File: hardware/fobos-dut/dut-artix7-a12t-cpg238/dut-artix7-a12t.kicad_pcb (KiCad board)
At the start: 4 copper layers, 88.9 x 76.2 mm, 204 parts, among them J1 Target, J10 Barrel_Jack_Switch, J2 Pmod 2x6, J3 575-8, J4 Glitch, J5 Conn_01x02, J6 Measure, J7 0878321420, J8 575-8, J9 Measure, Q1 FDS9435A, Q2 MMBT3904, Q3 BSS138, Q4 BSS138, Q5 BSS138, Q6 BSS138, Q7 BSS138, Q8 MMBT3904, SW1 SW_DIP_x03, SW2 SW_DIP_x03, U1 XC7A12T-CPG238, U10 SP3003-04ATG, U11 SP3003-04ATG, U2 SP3003-04ATG, U3 SP3003-04ATG, U4 SP3003-04ATG, U5 INA225, U6 BGA2801, U7 TS3A5018DBQR, U8 LTC3569EFE#PBF, U9 IS25LP256D-JMLE

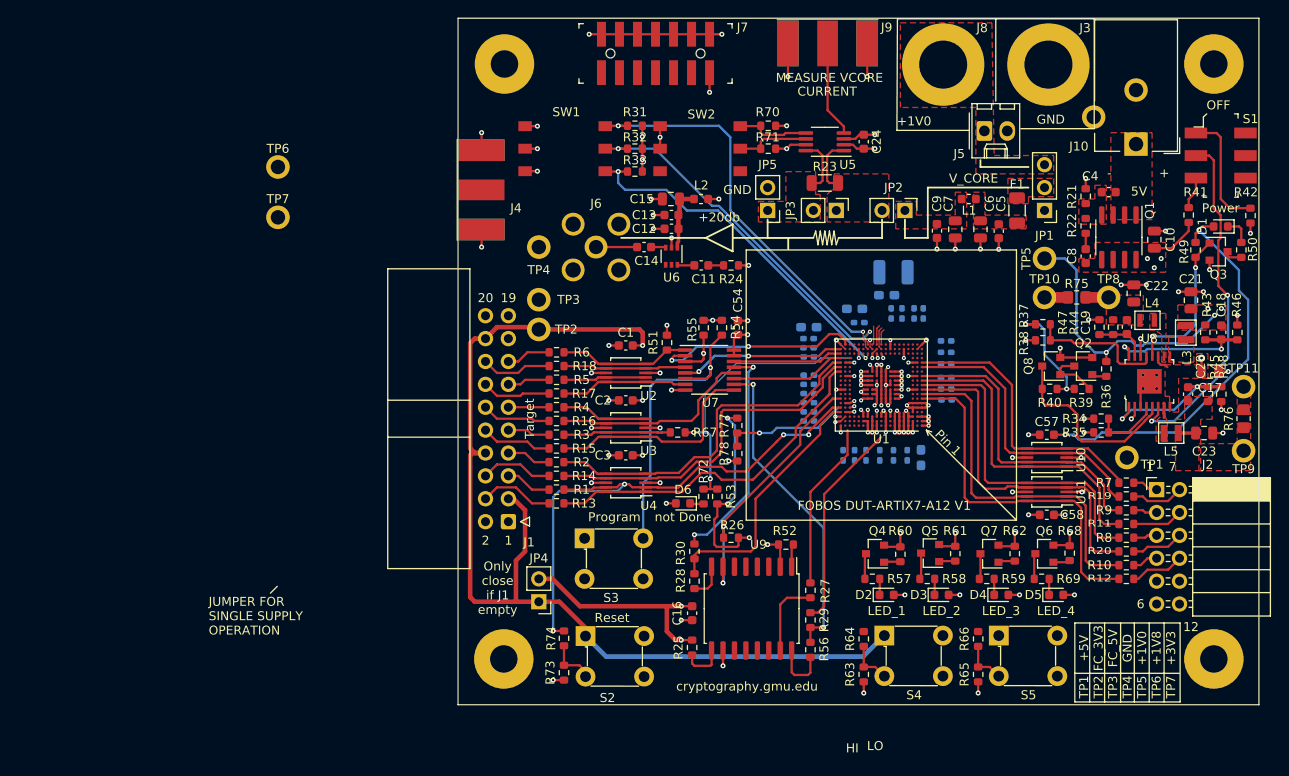
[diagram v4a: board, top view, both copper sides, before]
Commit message: All signals routed, need to route power
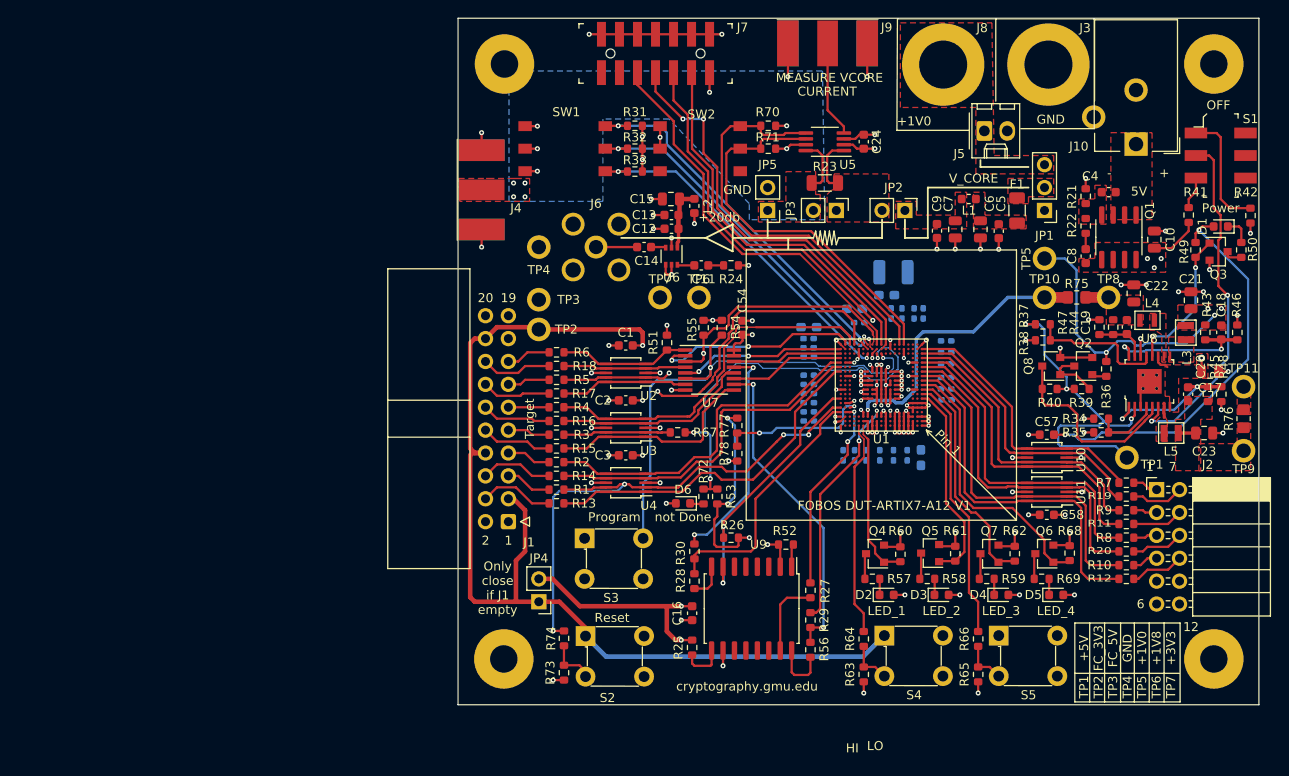
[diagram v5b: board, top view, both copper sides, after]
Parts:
- moved TP6 48.9 mm to (26.7, 27.4)
- moved TP7 43.3 mm to (22.4, 27.4)
- moved L2 1.07 mm to (26.2, 17.2), turned to 90 degrees
- moved C54 0.51 mm to (31.6, 30.7)
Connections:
- J7 pad 8: /FPGA Programming/TDO -> TDO
- R31 pad 2: /FPGA Programming/MODE_0 -> MODE_0
- SW1 pad 2: /FPGA Programming/MODE_0 -> MODE_0
- U1 pad A14: Net-(U1-PadA14) -> USER_LED_1
- U1 pad A15: Net-(U1-PadA15) -> USER_BTN_1
- U1 pad G1: JA10 -> USER_LED_2
- U1 pad H1: JA4 -> USER_BTN_2
- U1 pad J1: JA9 -> USER_LED_3
- U1 pad K1: JA3 -> USER_LED_4
- U1 pad L1: Net-(U1-PadL1) -> JA10
- U1 pad M1: Net-(U1-PadM1) -> JA4
- U1 pad N1: Net-(U1-PadN1) -> JA9
- U1 pad P1: Net-(U1-PadP1) -> JA3
- U1 pad R1: Net-(U1-PadR1) -> JA8
- U1 pad T1: Net-(U1-PadT1) -> JA2
- U1 pad U1: Net-(U1-PadU1) -> JA7
- U1 pad V1: Net-(U1-PadV1) -> JA1
- U1 pad V10: /FPGA Programming/TDO -> TDO
- U1 pad V13: /FPGA Programming/MODE_0 -> MODE_0
- U1 pad W14: Net-(U1-PadW14) -> MODE_0
- U1 pad W16: Net-(U1-PadW16) -> FD2C_HS
- U1 pad W17: Net-(U1-PadW17) -> FC2D_HS
- U1 pad W5: Net-(U1-PadW5) -> VCORE_CURRENT_GAIN_1
- U1 pad W6: Net-(U1-PadW6) -> VCORE_CURRENT_GAIN_0
- U1 pad W9: Net-(U1-PadW9) -> TDO
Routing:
- net +3V3: track 138.0 -> 251.0 mm
- net +1V8: track 6.10 -> 99.5 mm
- net /FPGA Programming/TCK: track 0.66 -> 62.6 mm, vias 1 -> 2
- net TDO: track 0.00 -> 46.5 mm, vias 0 -> 2
- net /FPGA Programming/MODE_0: track 46.0 -> 0.00 mm, vias 2 -> 0
- net /FPGA Programming/TDI: track 2.22 -> 44.9 mm
- net MODE_0: track 0.00 -> 41.4 mm, vias 0 -> 2
- net /FPGA Programming/TMS: track 1.78 -> 42.6 mm
- net VCORE_CURRENT_GAIN_0: track 8.25 -> 45.8 mm
- net FD2C_HS: track 9.17 -> 46.2 mm, vias 0 -> 2
- net VCORE_CURRENT_GAIN_1: track 8.17 -> 43.0 mm
- net FC2D_HS: track 9.60 -> 40.5 mm
- net USER_BTN_2: track 0.00 -> 29.5 mm
- net USER_LED_4: track 1.89 -> 31.0 mm
- net USER_BTN_1: track 0.00 -> 23.9 mm
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- added copper zone on B.Cu, net VCCINT
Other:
- net class Default: clearance 0.0762 -> 0.127
- rule trace_clearance: 0.0762 -> 0.127
- board text removed: "JUMPER FOR SINGLE SUPPLY OPERATION"

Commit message: Traces are routed and DRC errors are cleared, last remaining step is to place L3 power planes
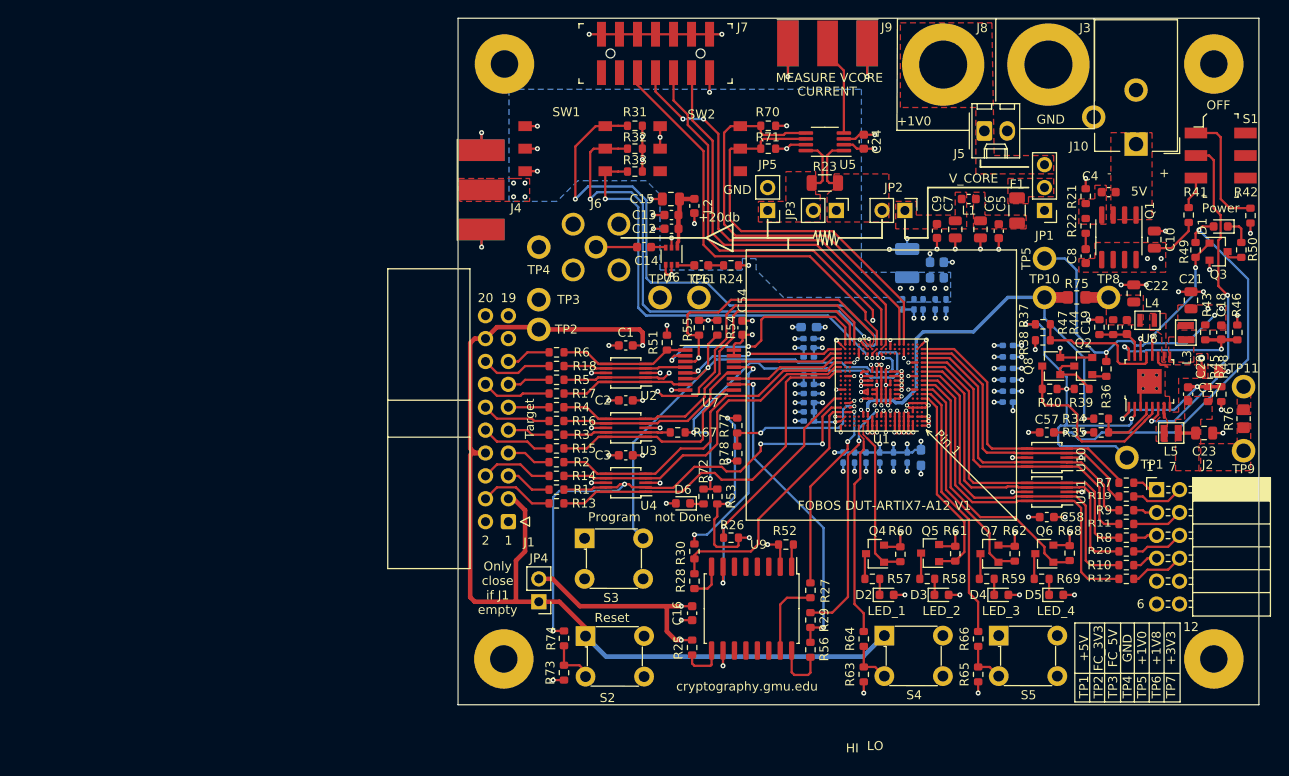
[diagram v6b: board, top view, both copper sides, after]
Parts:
- moved C55 9.42 mm to (52.4, 24.3), turned to 90 degrees
- moved C47 6.93 mm to (53.9, 24.3), turned to 90 degrees
- moved C49 6.88 mm to (61.0, 32.7)
- moved C50 6.88 mm to (61.0, 35.2)
- moved C52 6.88 mm to (61.0, 34.0)
- moved C48 6.86 mm to (61.0, 36.5)
- moved C51 6.86 mm to (61.0, 37.8)
- moved C53 6.80 mm to (61.0, 39.0)
- moved C44 6.16 mm to (54.2, 28.1), turned to 270 degrees
- moved C56 5.23 mm to (49.3, 28.1), turned to 270 degrees
- moved C46 3.83 mm to (53.0, 28.1), turned to 270 degrees
- moved C38 1.82 mm to (49.9, 23.6), turned to 90 degrees
- moved C41 1.44 mm to (50.6, 28.1), turned to 270 degrees
- moved C42 1.41 mm to (51.6, 28.1), turned to 270 degrees
- moved R54 0.51 mm to (28.8, 30.7)
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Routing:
- net +3V3: track 251.0 -> 317.2 mm, vias 23 -> 36
- net GND: track 177.4 -> 219.8 mm, vias 100 -> 129
- net +1V8: track 99.5 -> 126.8 mm, vias 3 -> 6
- net VCCINT: track 20.5 -> 46.8 mm, vias 8 -> 13
- net MODE_0: track 41.4 -> 62.8 mm
- net /FPGA Programming/MODE_1: track 40.7 -> 54.4 mm
- net /FPGA Programming/MODE_2: track 39.0 -> 49.2 mm
- net FC_DIO3_MUX: track 23.0 -> 26.9 mm
- net SW_INIT_B: track 28.1 -> 31.6 mm
- net SW_PROGRAM_B: track 57.3 -> 54.1 mm
- net FC2D_HS: track 40.5 -> 43.5 mm
- net FD2C_CLK: track 39.1 -> 41.6 mm
- net /FPGA Programming/TDI: track 44.9 -> 47.4 mm
- net /FPGA Programming/TMS: track 42.6 -> 44.9 mm
- net TDO: track 46.5 -> 48.8 mm
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- added copper zone on In2.Cu, net VCCINT

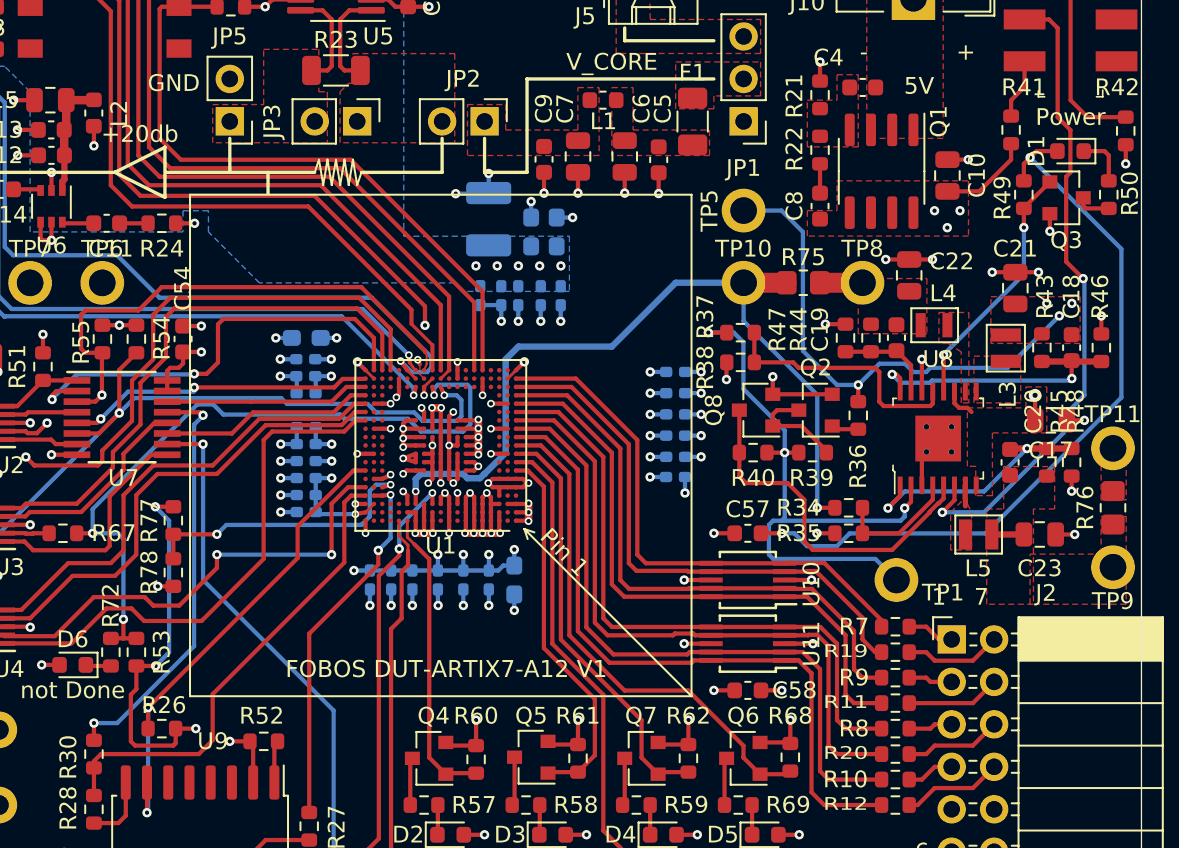
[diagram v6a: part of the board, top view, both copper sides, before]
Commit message: Poured copper planes for L2 Added second 3 mil trace to Pad V12
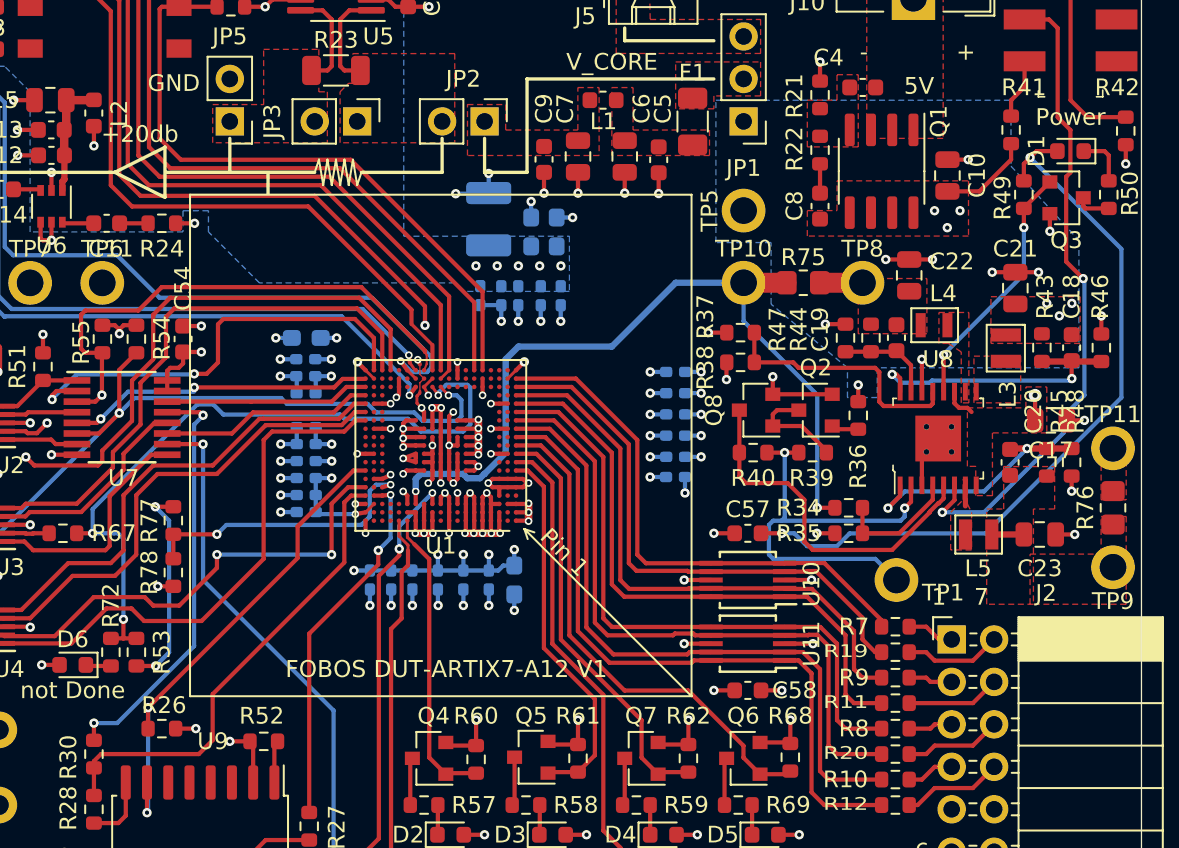
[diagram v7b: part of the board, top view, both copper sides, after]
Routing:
- net +3V3: track 317.2 -> 96.9 mm
- net FC_5V: track 134.8 -> 0.00 mm
- net FC_3V3: track 337.5 -> 219.4 mm
- net +5V: track 89.5 -> 38.8 mm
- net +1V8: track 126.8 -> 87.9 mm
- net +1V0: track 35.8 -> 1.00 mm
- net GND: track 219.8 -> 221.9 mm
- added copper zone on B.Cu, net +1V0
- added copper zone on In2.Cu, net +1V8
- added copper zone on In2.Cu, net +3V3
- added copper zone on In2.Cu, net +5V
- added copper zone on In2.Cu, net FC_3V3
- added copper zone on In2.Cu, net FC_5V

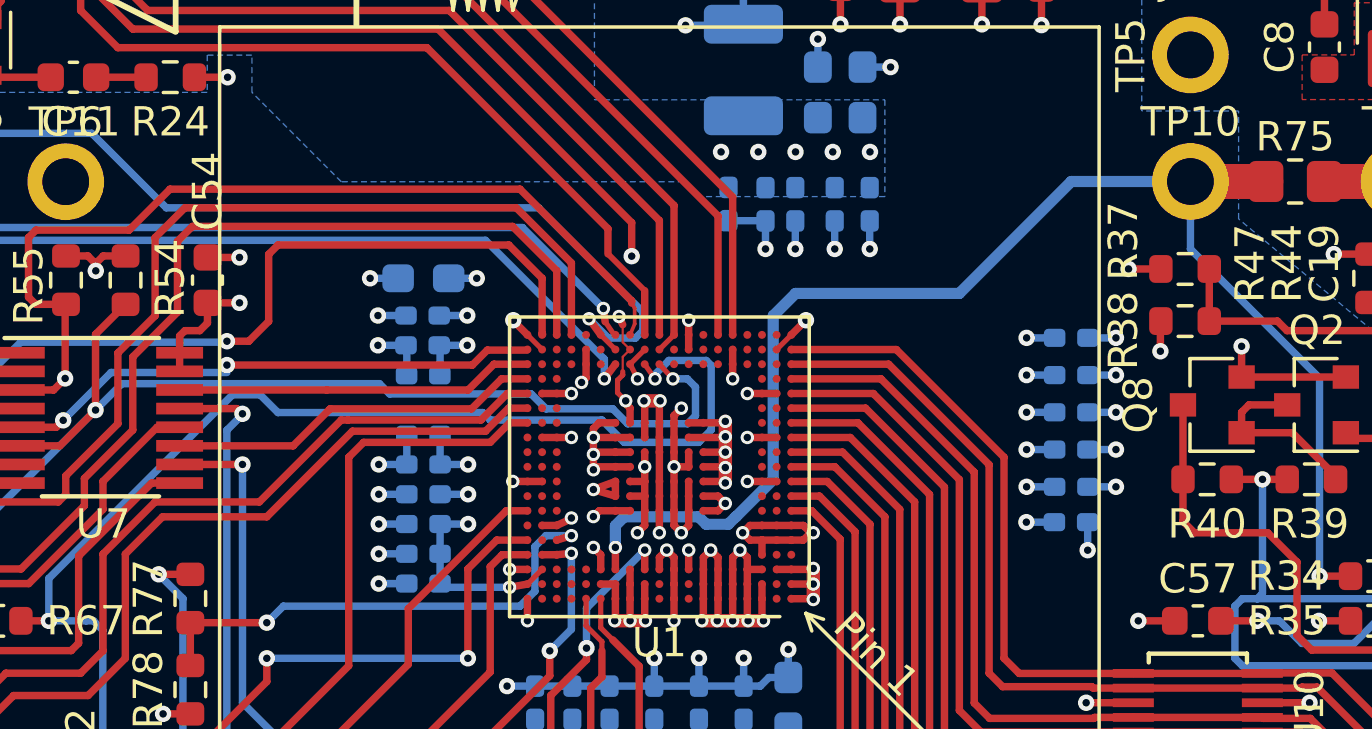
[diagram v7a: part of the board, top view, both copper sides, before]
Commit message: Modified L2 power planes Fixed bottom silkscreen overlap with component pads
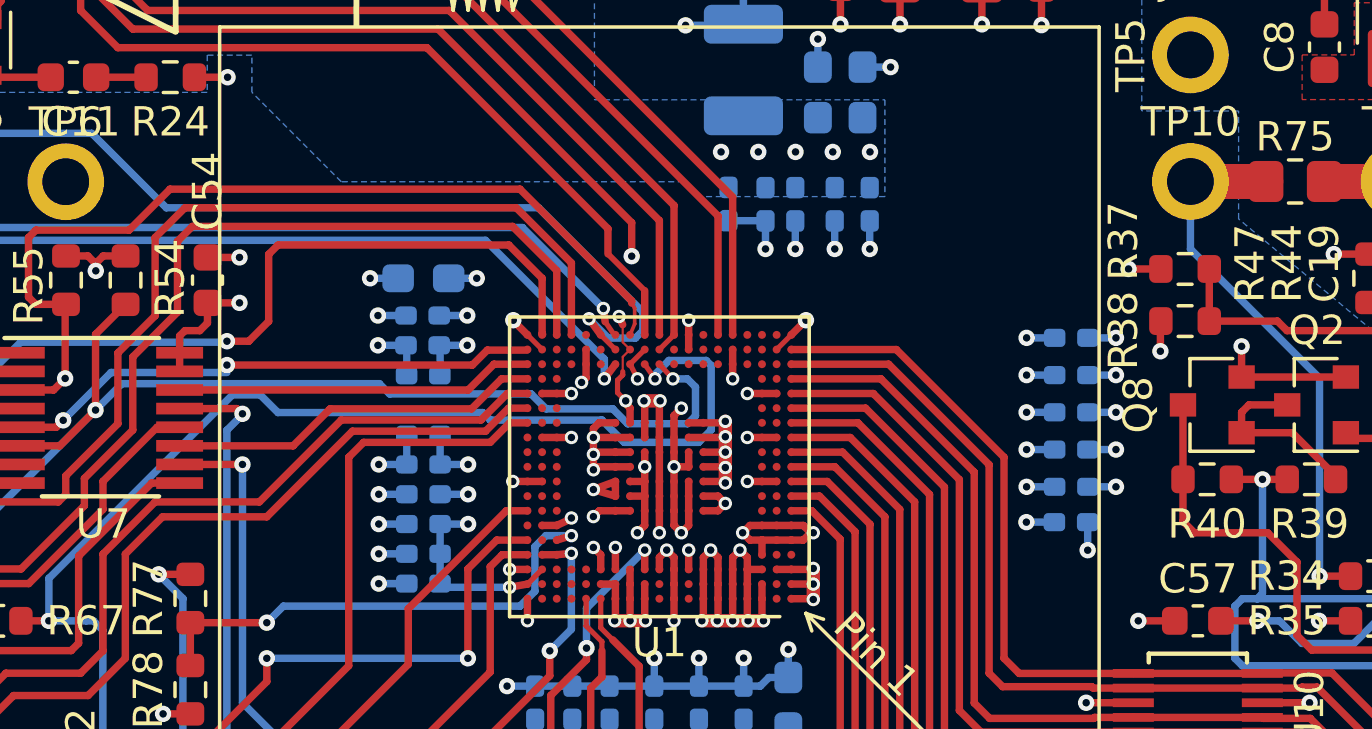
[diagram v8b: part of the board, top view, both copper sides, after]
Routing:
- net +1V8: track 87.9 -> 31.0 mm
- net VCCINT: track 46.8 -> 51.0 mm
